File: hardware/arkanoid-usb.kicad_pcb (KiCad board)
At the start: 2 copper layers, 38.6 x 61.2 mm, 20 parts, among them J1 AVR-ISP-6, J2 Conn_01x15, J3 USB_B, J4 Conn_01x03, U1 ATtiny861-20PU, Y1 20MHz

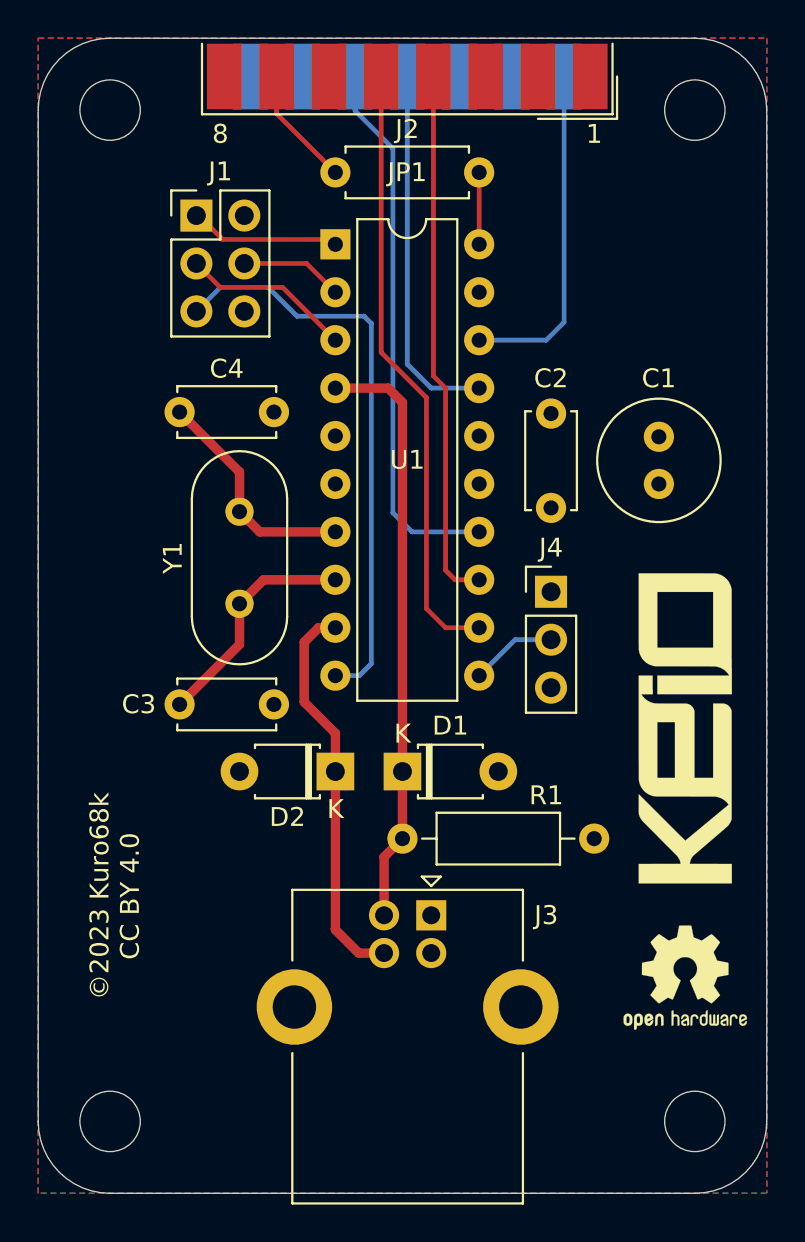
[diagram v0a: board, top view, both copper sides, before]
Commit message: Corrected programming header
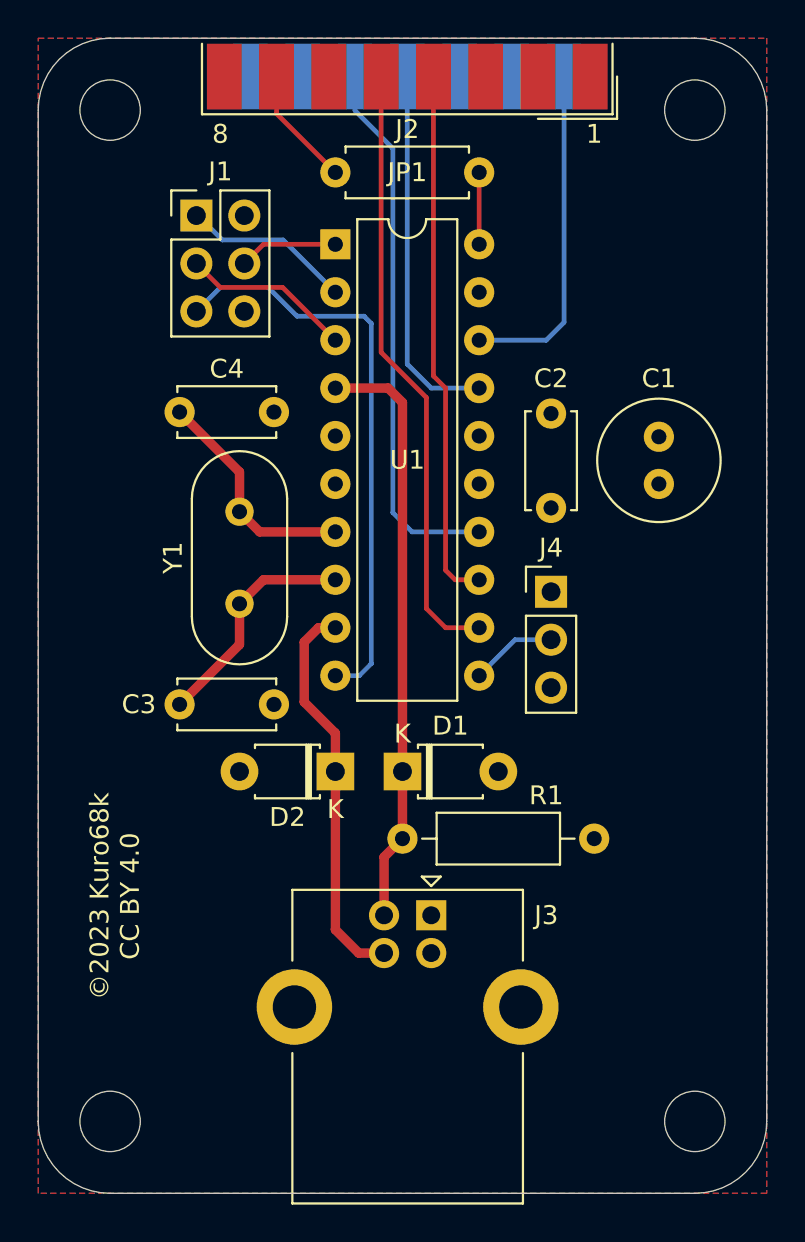
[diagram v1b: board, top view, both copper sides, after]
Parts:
- removed G***: LOGO, Keio:logo2_16x5mm_top_silk
- removed REF**: OSHW-Logo2_7.3x6mm_SilkScreen, Symbol:OSHW-Logo2_7.3x6mm_SilkScreen
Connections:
- J1 pad 1: /MOSI -> /MISO
- J1 pad 4: /MISO -> /MOSI
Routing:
- net /MISO: track 5.46 -> 9.05 mm
- net /MOSI: track 8.00 -> 5.25 mm
